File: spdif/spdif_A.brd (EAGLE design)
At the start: 70 x 70 mm, 66 parts, among them T1 DA101MC, T2 DA101MC, U1 NC7SZ175, U2 FIN1001, U3 FIN1002, U4 NC7SZ175, U5 NC7SZ175, U6 FIN1002

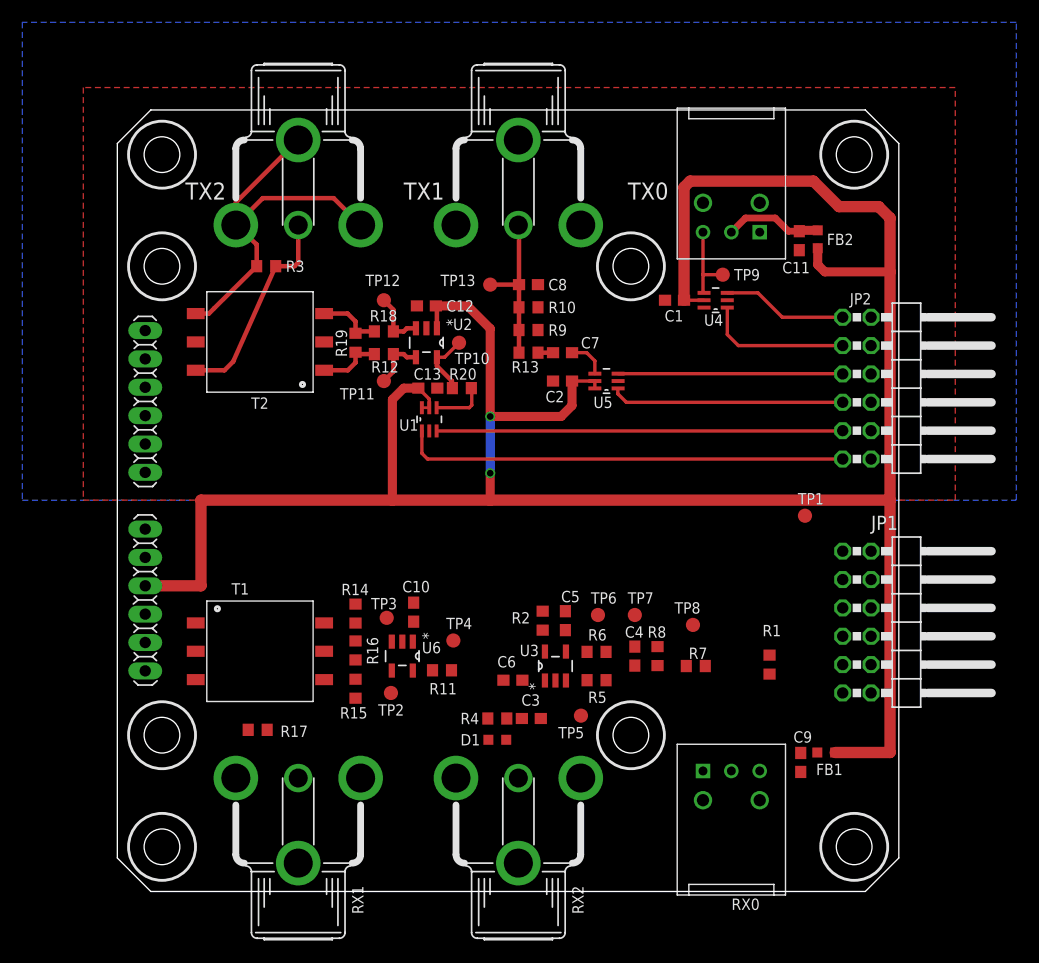
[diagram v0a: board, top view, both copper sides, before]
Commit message: spdif: finished PCB
Signed-off-by: malo <pavol.malosek@gmail.com>
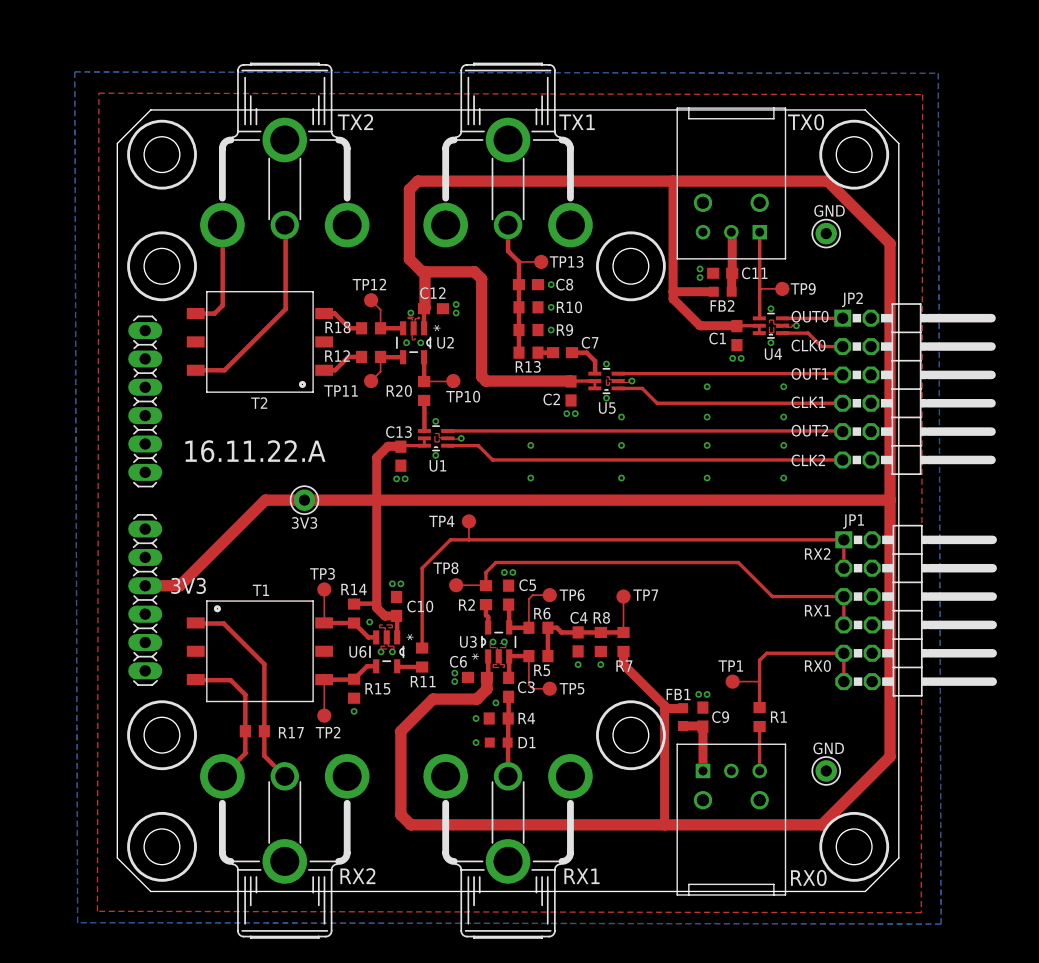
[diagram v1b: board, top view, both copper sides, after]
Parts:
- removed R16: 100R, 0603, rcl:R0603
- removed R19, R3: 75R, 0603, rcl:R0603
- added 3V3, GND, GND33: TEST-22-MULTICOMP, 25cmsquare:TEST_1MM
- R12, R18: value 220R, 0603 -> 36R, 0603
- moved TP8 21.5 mm to (30.4, 27.4)
- moved RX2 20.9 mm to (15.0, 10.3)
- moved RX1 18.8 mm to (35.0, 10.3)
- moved TP1 16.2 mm to (55.1, 18.8)
- moved FB1 13.2 mm to (50.7, 15.6), turned to 90 degrees
- moved TP4 10.8 mm to (31.5, 33.1)
- moved FB2 9.72 mm to (54.2, 53.7), turned to 180 degrees
- moved C9 9.66 mm to (52.5, 15.6), turned to 270 degrees
- moved C11 7.45 mm to (54.2, 55.4), turned to 0 degrees
- moved R7 6.83 mm to (45.3, 22.4), turned to 270 degrees
- moved C13 6.56 mm to (25.4, 39.0), turned to 90 degrees
- moved C1 6.43 mm to (55.5, 49.8), turned to 90 degrees
- moved TP2 6.31 mm to (18.5, 15.7)
- moved TP3 6.14 mm to (18.5, 27.1)
- moved R5 5.64 mm to (37.7, 21.1)
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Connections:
- net +3V3: now also 3V3.1
- net DA_N: no longer R19.1
- net DA_P: no longer R19.2
- net GND: now also GND.1, GND33.1, RX1.20, RX1.21, RX1.22, TX0.3; no longer RX2.20, RX2.21, RX2.22, TX0.1
- net N$16: no longer R16.2
- net N$17: no longer R16.1
- net N$20: now also RX2.21; no longer RX1.20, RX1.21, RX1.22
- net N$21: now also RX2.1; no longer RX1.1
- net N$6: now also RX1.1; no longer RX2.1
- net SPDIF_IN_0: now also JP1.11, JP1.9; no longer JP1.1, JP1.3
- net SPDIF_IN_1: now also R2.2, TP8.TP; no longer R11.2, TP4.TP
- net SPDIF_IN_2: now also JP1.1, JP1.3, R11.2, TP4.TP; no longer JP1.11, JP1.9, R2.2, TP8.TP
- net TX0_IN: now also TX0.1; no longer TX0.3
- net TX2_N: no longer R3.2, TX2.21, TX2.22
- net TX2_P: no longer R3.1
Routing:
- net +3V3: track 217.7 -> 334.4 mm, vias 2 -> 0
- net SPDIF_IN_2: track 0.00 -> 50.2 mm
- net SPDIF_IN_1: track 0.00 -> 40.1 mm
- net TX2_N: track 34.8 -> 9.91 mm
- net N$21: track 0.00 -> 18.5 mm
- net SPDIF_IN_0: track 0.00 -> 17.0 mm
- net N$20: track 0.00 -> 13.2 mm
- net N$11: track 0.00 -> 12.7 mm
- net N$12: track 0.00 -> 8.46 mm
- net N$16: track 0.00 -> 8.39 mm
- net N$4: track 0.00 -> 8.30 mm
- net N$17: track 0.00 -> 8.20 mm
- net CLK_0: track 13.2 -> 5.88 mm
- net N$6: track 0.00 -> 7.18 mm
- net SPDIF_OUT_0: track 11.2 -> 5.39 mm
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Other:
- board text added: "16.11.22.A"
- board text added: "3V3"
- board text added: "CLK0"
- board text added: "CLK1"
- board text added: "CLK2"
- board text added: "GND"
- board text added: "OUT0"
- board text added: "OUT1"
- board text added: "OUT2"
- board text added: "RX0"
- board text added: "RX1"
- board text added: "RX2"
